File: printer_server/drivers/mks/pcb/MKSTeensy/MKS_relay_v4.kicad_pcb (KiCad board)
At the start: 2 copper layers, 111.3 x 68.1 mm, 67 parts, among them J1 Conn_01x03, J10 Conn_01x02, J11 Conn_01x02, J12 Conn_01x02, J13 Conn_01x02, J14 Conn_01x02, J15 Conn_01x02, J16 Conn_01x02, J17 Conn_01x02, J18 Conn_01x02, J19 Conn_01x02, J2 Conn_01x04, J20 Conn_01x02, J21 Conn_01x02, J22 DB25_Receptacle_MountingHoles, J3 Barrel_Jack_PTH, J4 Conn_01x02, J5 Conn_01x02, J6 Conn_01x02, J7 Conn_01x02, J8 Conn_01x02, J9 Conn_01x02, Q1 IRLZ34N, Q2 IRLZ34N, Q3 IRLZ34N, Q4 IRLZ34N, Q5 IRLZ34N, Q6 IRLZ34N, Q7 IRLZ34N, Q8 IRLZ34N, Q9 IRLZ34N, U1 Teensy4.0

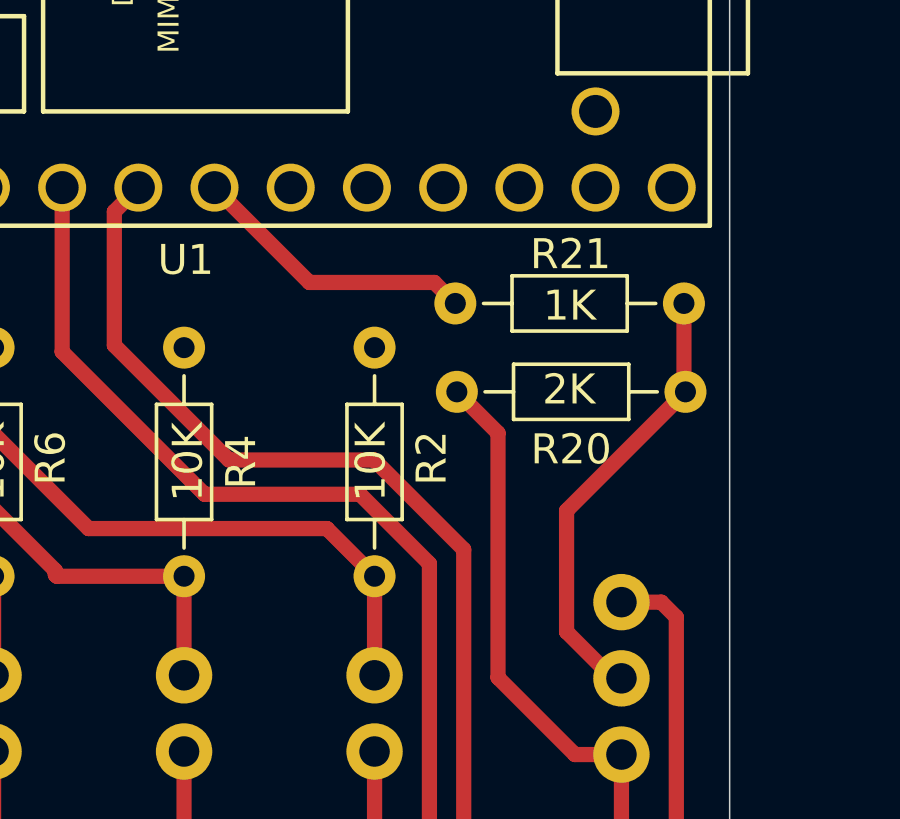
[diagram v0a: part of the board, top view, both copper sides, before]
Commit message: Fix voltage divider in  MKS PCB
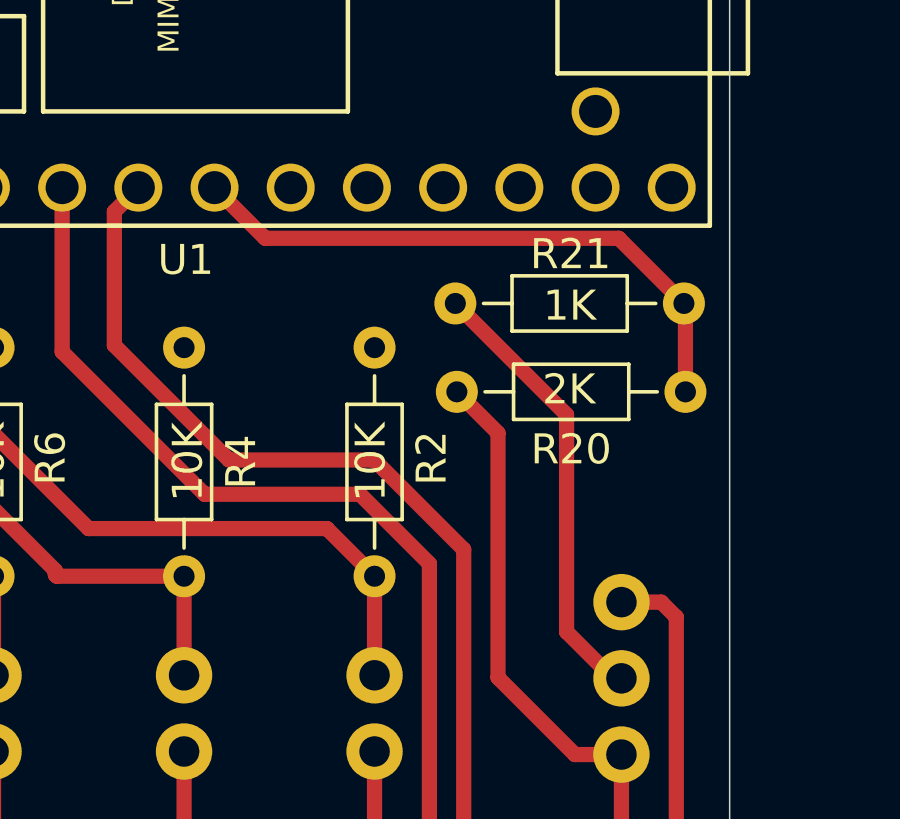
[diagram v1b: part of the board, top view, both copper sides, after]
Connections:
- R20 pad 1: Net-(J1-Pin_2) -> Net-(U1-20_A6_TX5_LRCLK1)
- R21 pad 1: Net-(U1-20_A6_TX5_LRCLK1) -> Net-(J1-Pin_2)
- R21 pad 2: Net-(J1-Pin_2) -> Net-(U1-20_A6_TX5_LRCLK1)
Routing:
- net Net-(U1-20_A6_TX5_LRCLK1): track 9.63 -> 20.3 mm
